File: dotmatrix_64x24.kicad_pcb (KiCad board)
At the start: 2 copper layers, 180 x 100 mm, 841 parts, among them CON1 BARREL_JACK, P1 CONN_01X09, P2 CONN_01X09, P3 CONN_01X04, P4 CONN_01X03, P5 USB_OTG, P6 CONN_01X03, Q1 NJL7302L-F3, Q3 Q_NPN_BCE RN5006, SW1 SW_PUSH_SMALL_H, SW2 SW_PUSH_SMALL_H, SW3 SW_PUSH_SMALL_H, SW4 SW_PUSH_SMALL_H, SW5 SW_PUSH_SMALL_H, SW6 SW_PUSH_SMALL_H, SW7 SW_PUSH_SMALL_H, SW8 SW_PUSH_SMALL_H, U1 WROOM-02, U10 LED1642GW, U11 LED1642GW, U12 AE-BME280, U13 TPS54426, U14 NJU7223, U15 DS1307, U16 CH340G, U17 OSRB38C9AA, U18 BME280, U2 74HC595-alt-vdd, U3 TD62783, U4 74HC595-alt-vdd, U5 TD62783, U6 LED1642GW, U7 74HC595-alt-vdd, U8 TD62783, U9 LED1642GW, X1 CRYSTAL_SMD, Y1 12MHz

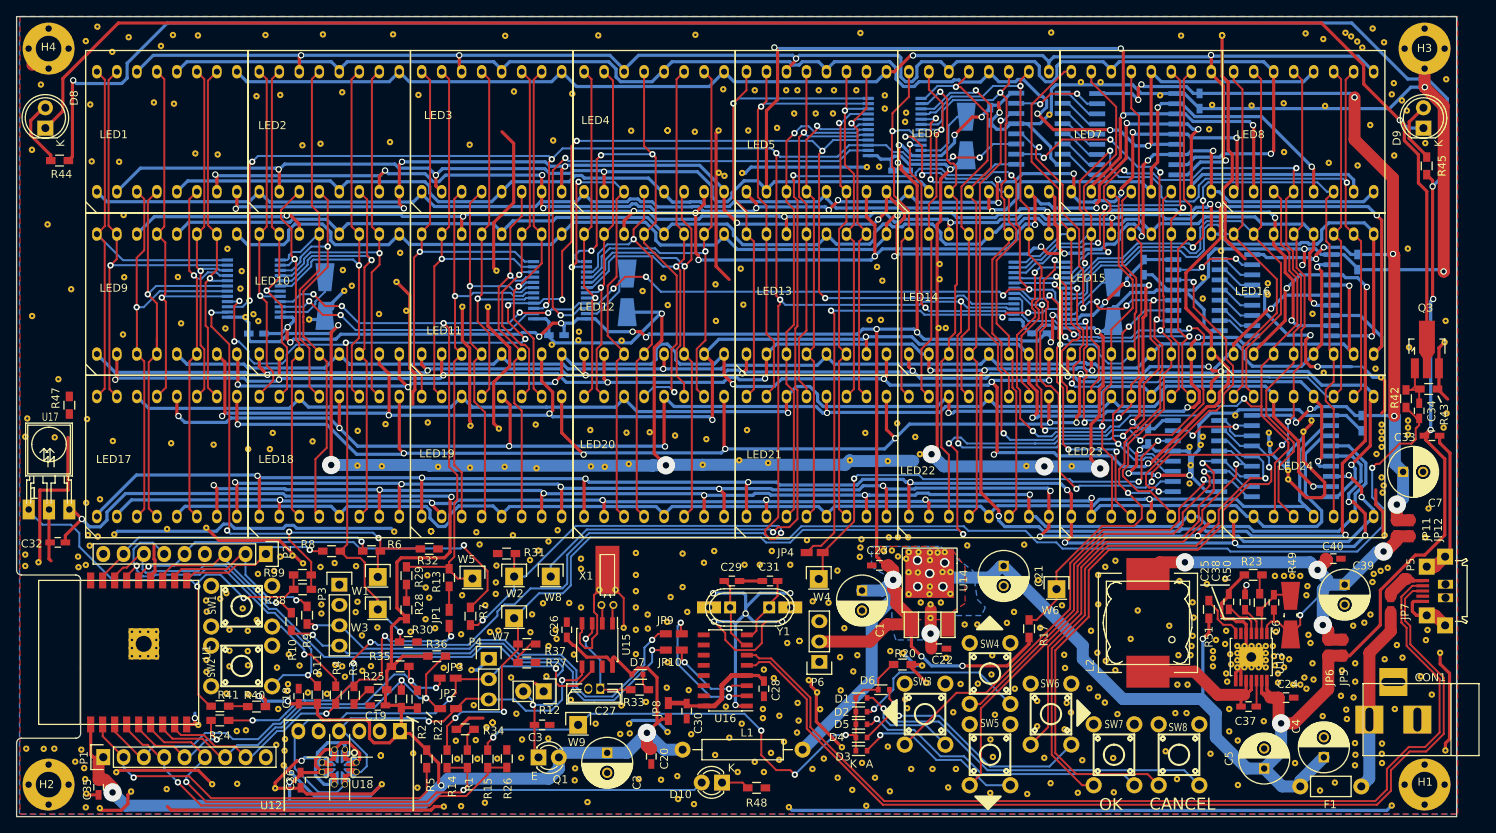
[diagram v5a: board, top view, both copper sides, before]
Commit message: Modified to improve impedance of the reference voltage of LED Driver's current setting R
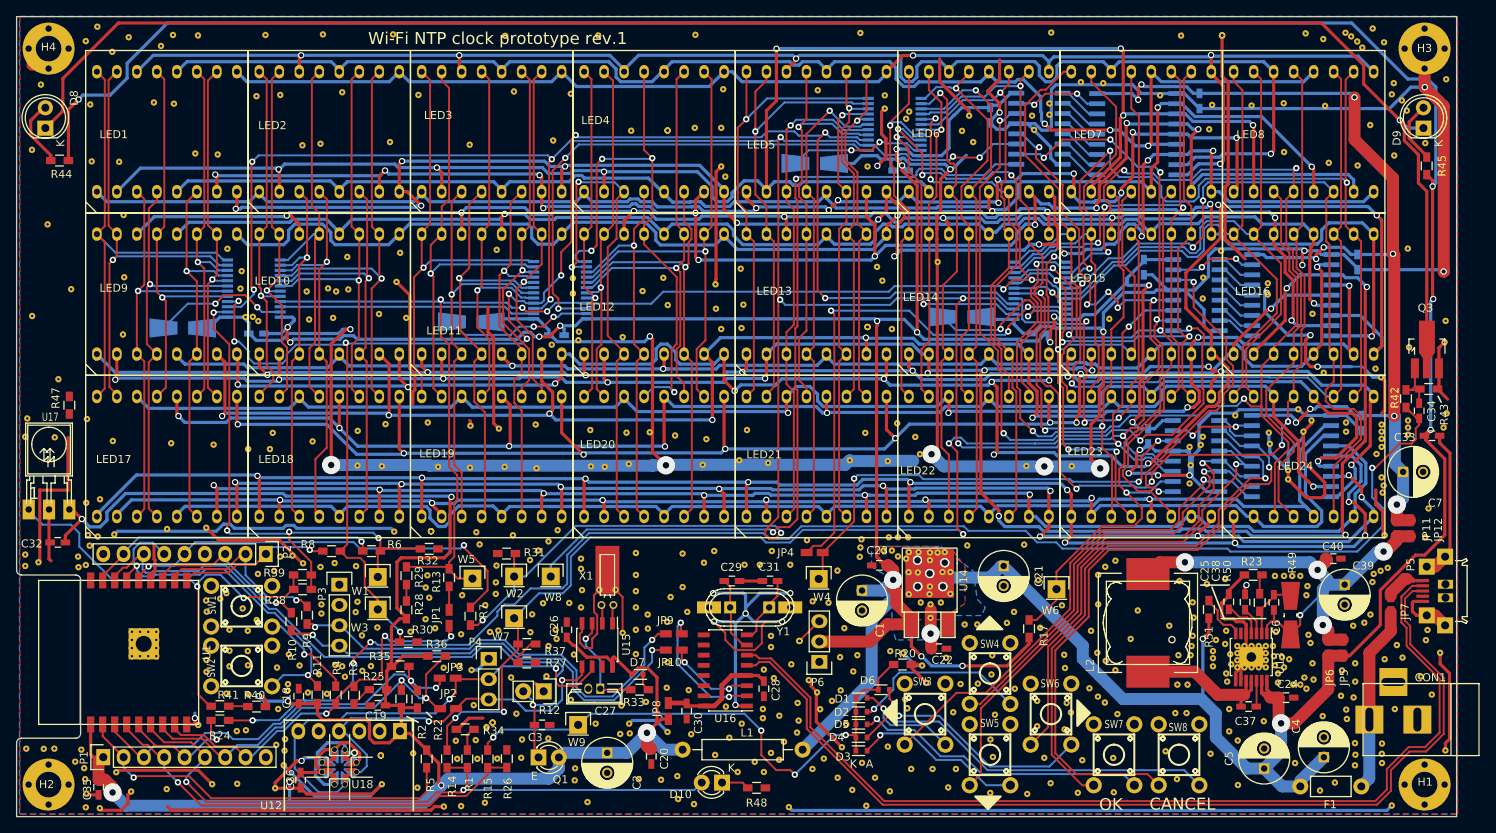
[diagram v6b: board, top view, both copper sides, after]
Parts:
- removed the REF** at (104.3, 21.2)
- removed the REF** at (108.2, 21.2)
- removed the REF** at (109.6, 21.2)
- removed the REF** at (107.1, 25.9)
- removed the REF** at (111.9, 24.1)
- removed the REF** at (114.0, 24.1)
- removed the REF** at (112.3, 21.2)
- removed the REF** at (114.2, 21.2)
- removed the REF** at (117.0, 21.2)
- removed the REF** at (72.0, 43.8)
- removed the REF** at (67.7, 48.3)
- removed the REF** at (70.9, 48.3)
- removed the REF** at (38.1, 51.0)
- removed the REF** at (32.2, 44.6)
- removed the REF** at (120.0, 49.9)
- removed the REF** at (127.4, 44.8)
- removed the REF** at (103.5, 26.2)
- removed the REF** at (32.6, 50.3)
- removed the REF** at (109.2, 24.1)
- removed the REF** at (119.8, 30.8)
- removed the REF** at (118.6, 49.9)
- removed the REF** at (127.4, 42.9)
- removed the REF** at (128.1, 50.9)
- removed the REF** at (127.3, 50.9)
- removed the REF** at (118.3, 30.8)
- removed the REF** at (102.7, 31.5)
- added REF**: stitch-via-0.6mm, components:stitch-via-0.8mm, F.Cu at (141.1, 22.9)
- added REF**: stitch-via-0.6mm, components:stitch-via-0.8mm, F.Cu at (102.6, 50.9)
- added REF**: stitch-via-0.6mm, components:stitch-via-0.8mm, F.Cu at (100.1, 51.1)
- added REF**: stitch-via-0.6mm, components:stitch-via-0.8mm, F.Cu at (81.5, 46.6)
- added REF**: stitch-via-0.6mm, components:stitch-via-0.8mm, F.Cu at (81.5, 44.7)
- added REF**: stitch-via-0.6mm, components:stitch-via-0.8mm, F.Cu at (112.1, 21.2)
- added REF**: stitch-via-0.6mm, components:stitch-via-0.8mm, F.Cu at (48.3, 46.4)
- added REF**: stitch-via-0.6mm, components:stitch-via-0.8mm, F.Cu at (127.1, 42.7)
- added REF**: stitch-via-0.6mm, components:stitch-via-0.8mm, F.Cu at (148.6, 49.8)
- added REF**: stitch-via-0.6mm, components:stitch-via-0.8mm, F.Cu at (131.1, 24.4)
- added REF**: stitch-via-0.6mm, components:stitch-via-0.8mm, F.Cu at (130.2, 26.3)
- added REF**: stitch-via-0.6mm, components:stitch-via-0.8mm, F.Cu at (139.2, 26.2)
- added REF**: stitch-via-0.6mm, components:stitch-via-0.8mm, F.Cu at (53.3, 42.0)
- added REF**: stitch-via-0.6mm, components:stitch-via-0.8mm, F.Cu at (51.6, 49.7)
- added REF**: stitch-via-0.6mm, components:stitch-via-0.8mm, F.Cu at (172.2, 61.1)
- added REF**: stitch-via-0.6mm, components:stitch-via-0.8mm, F.Cu at (178.2, 63.9)
- added REF**: stitch-via-0.6mm, components:stitch-via-0.8mm, F.Cu at (178.2, 62.7)
- added REF**: stitch-via-0.6mm, components:stitch-via-0.8mm, F.Cu at (82.7, 83.7)
- added REF**: stitch-via-0.6mm, components:stitch-via-0.8mm, F.Cu at (108.8, 93.0)
- added REF**: stitch-via-0.6mm, components:stitch-via-0.8mm, F.Cu at (106.3, 90.8)
- added REF**: stitch-via-0.6mm, components:stitch-via-0.8mm, F.Cu at (113.9, 97.5)
- added REF**: stitch-via-0.6mm, components:stitch-via-0.8mm, F.Cu at (115.7, 100.5)
- added REF**: stitch-via-0.6mm, components:stitch-via-0.8mm, F.Cu at (138.9, 24.4)
- added REF**: stitch-via-0.6mm, components:stitch-via-0.8mm, F.Cu at (123.3, 98.5)
- added REF**: stitch-via-0.6mm, components:stitch-via-0.8mm, F.Cu at (131.6, 27.7)
- added REF**: stitch-via-0.6mm, components:stitch-via-0.8mm, F.Cu at (118.4, 30.7)
- added REF**: stitch-via-0.6mm, components:stitch-via-0.8mm, F.Cu at (72.0, 41.1)
- added REF**: stitch-via-0.6mm, components:stitch-via-0.8mm, F.Cu at (121.4, 51.1)
- added REF** (x2): stitch-via-0.6mm, components:stitch-via-0.8mm, F.Cu at (118.4, 50.8)
- moved R18 19.8 mm to (68.8, 50.2), turned to 0 degrees
- moved R19 19.3 mm to (111.8, 30.4), turned to 0 degrees
- moved R21 19.0 mm to (130.2, 49.5), turned to 0 degrees
- moved R16 18.2 mm to (32.8, 50.9), turned to 0 degrees
- moved REF** 2.94 mm to (50.9, 46.0)
- moved REF** 2.22 mm to (106.3, 89.4)
- moved REF** 1.52 mm to (99.4, 48.5)
- moved REF** 1.02 mm to (51.9, 46.4)
- moved REF** 0.89 mm to (60.7, 49.7)
- moved REF** 0.84 mm to (100.1, 30.7)
- moved REF** 0.65 mm to (87.8, 89.0)
- moved REF** 0.63 mm to (53.5, 46.1)
- moved REF** 0.48 mm to (96.8, 25.9)
- moved REF** 0.47 mm to (100.1, 25.9)
- moved REF** 0.45 mm to (87.8, 52.1)
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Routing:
- net GND: track 1142.7 -> 1116.7 mm, vias 29 -> 30
- net Net-(R21-Pad1): track 7.90 -> 21.3 mm, vias 0 -> 2
- net Net-(R18-Pad1): track 7.89 -> 18.6 mm, vias 0 -> 2
- net Net-(R19-Pad1): track 8.64 -> 17.3 mm, vias 0 -> 2
- net Net-(R16-Pad1): track 8.66 -> 17.2 mm, vias 0 -> 2
- net /Sheet57A04605/r20: track 182.7 -> 189.2 mm
- net /Sheet57A04605/COLLATCH: track 201.8 -> 206.2 mm
- net /Sheet57A04605/c61: track 85.3 -> 89.6 mm
- net Net-(U10-Pad22): track 34.1 -> 37.6 mm
- net /Sheet57A04605/r3: track 199.9 -> 203.3 mm
- net VCC: track 385.0 -> 381.7 mm
- net /Sheet57A04605/c11: track 51.8 -> 48.8 mm
- net /Sheet57A04605/COLCLK: track 338.9 -> 341.8 mm
- net /Sheet57A04605/c52: track 72.1 -> 74.5 mm
- net /Sheet57A04605/c19: track 51.4 -> 53.8 mm
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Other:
- board text added: "Wi-Fi NTP clock prototype rev.1"

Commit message: Track cleanup
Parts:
- added REF**: stitch-via-0.6mm, components:stitch-via-0.8mm, F.Cu at (165.1, 23.1)
- moved REF** 1.66 mm to (87.9, 90.7)
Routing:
- net /ESPVDD: track 282.3 -> 280.7 mm
- net GND: track 1116.7 -> 1118.2 mm

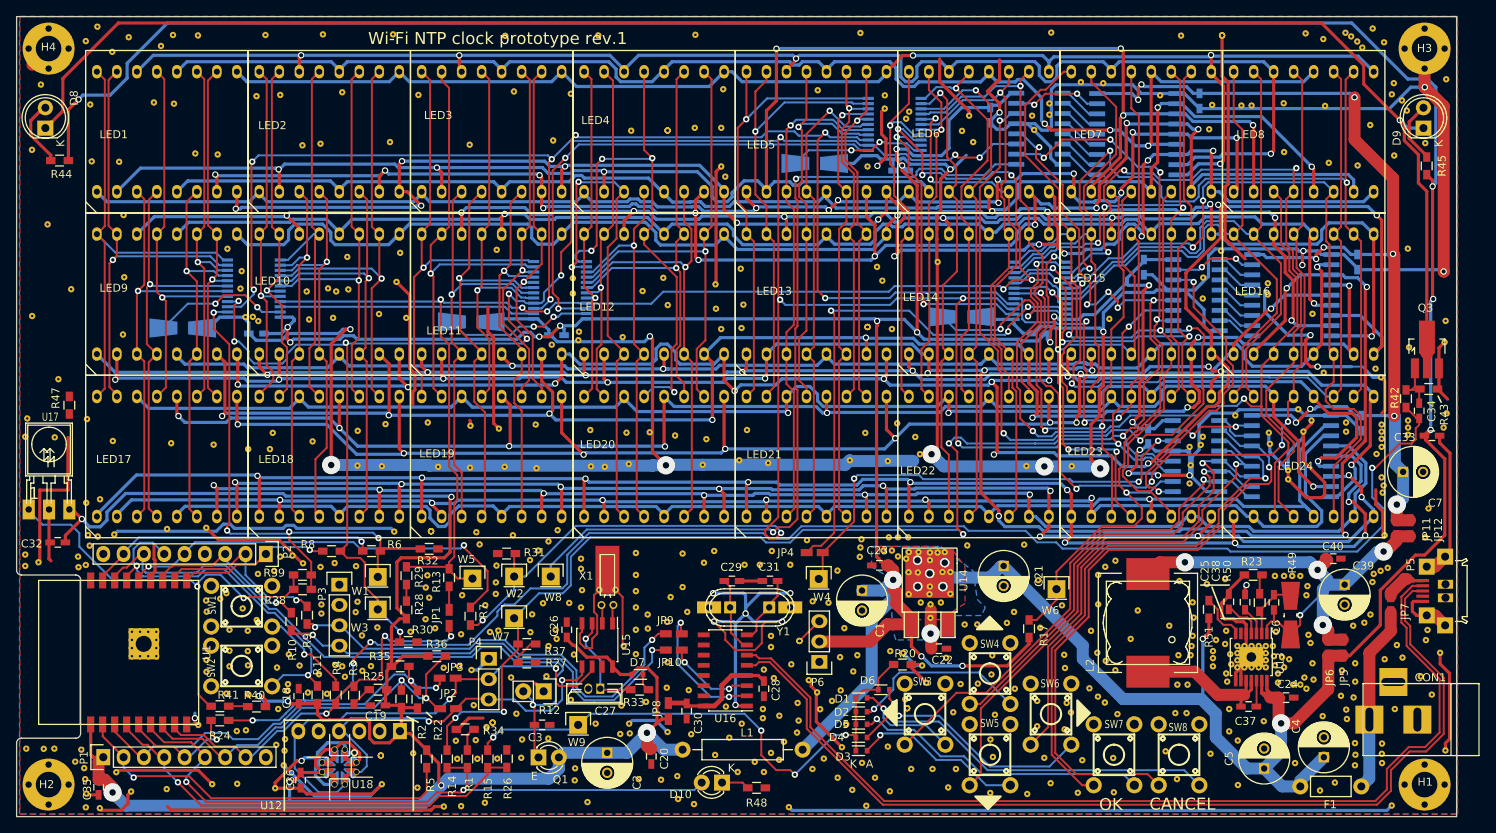
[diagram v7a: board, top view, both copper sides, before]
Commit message: Improved hand-solderbility and fixed traces
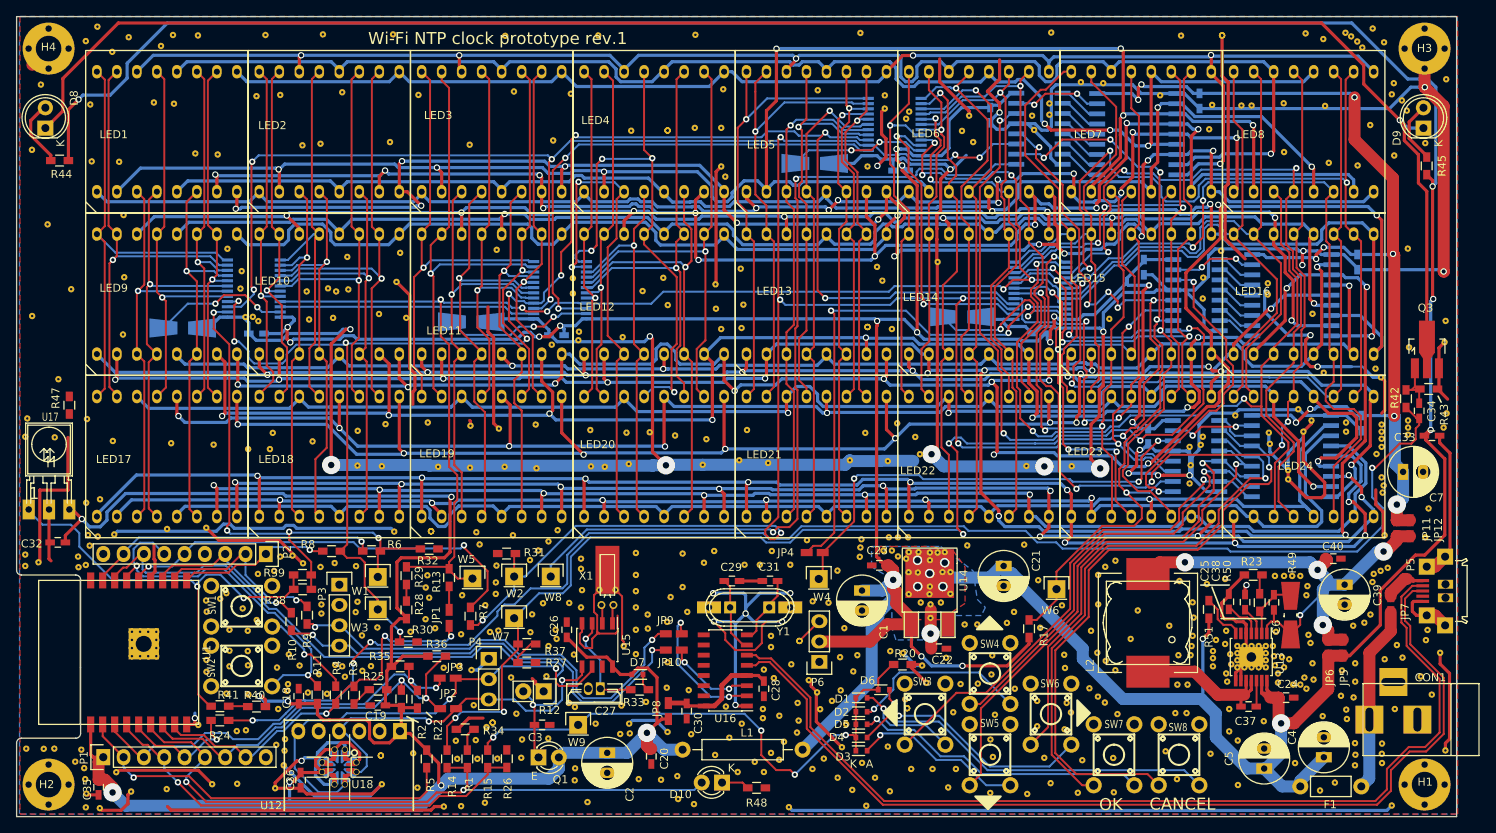
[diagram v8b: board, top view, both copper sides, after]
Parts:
- added REF**: stitch-via-0.6mm, components:stitch-via-0.8mm, F.Cu at (81.8, 98.3)
- C1, C2, C21, C39, C4, C5, C7: footprint Capacitors_ThroughHole:C_Radial_D6.3_L11.2_P2.5 -> components:C_Radial_D6.3_L11.2_P2.5_hand_soldering
- moved REF** 0.46 mm to (81.0, 97.8)
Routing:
- net GND: track 1118.2 -> 1125.0 mm
- net /Sheet57A04605/COLPWCLK: track 183.8 -> 179.9 mm
- net /Sheet57A04605/c45: track 63.8 -> 64.3 mm
